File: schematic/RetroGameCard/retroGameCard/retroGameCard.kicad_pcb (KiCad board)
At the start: 2 copper layers, 34 parts, among them IC1 STM32C562KET6, J2 Conn_01x04_Pin, J3 USB_C_Receptacle_USB2.0_16P, SW1 SW_Slide_DPDT, SW2 SW_SPDT, SW3 SW_Push, SW4 SW_Push, SW5 SW_Push, SW6 SW_Push, SW7 SW_Push, U1 MCP73831-2-OT, U2 AP2112K-3.3

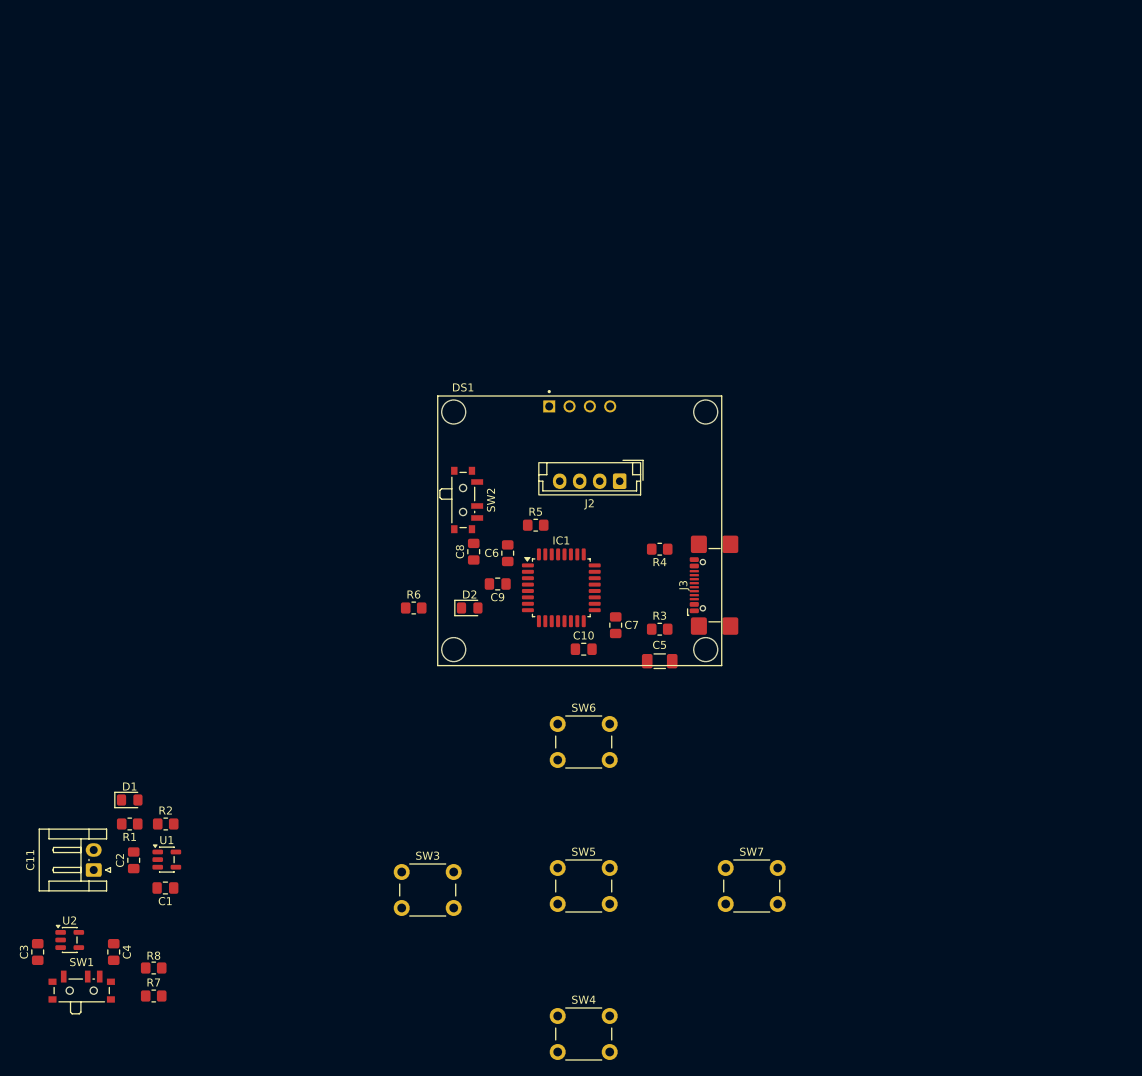
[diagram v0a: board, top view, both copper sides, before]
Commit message: changed layout
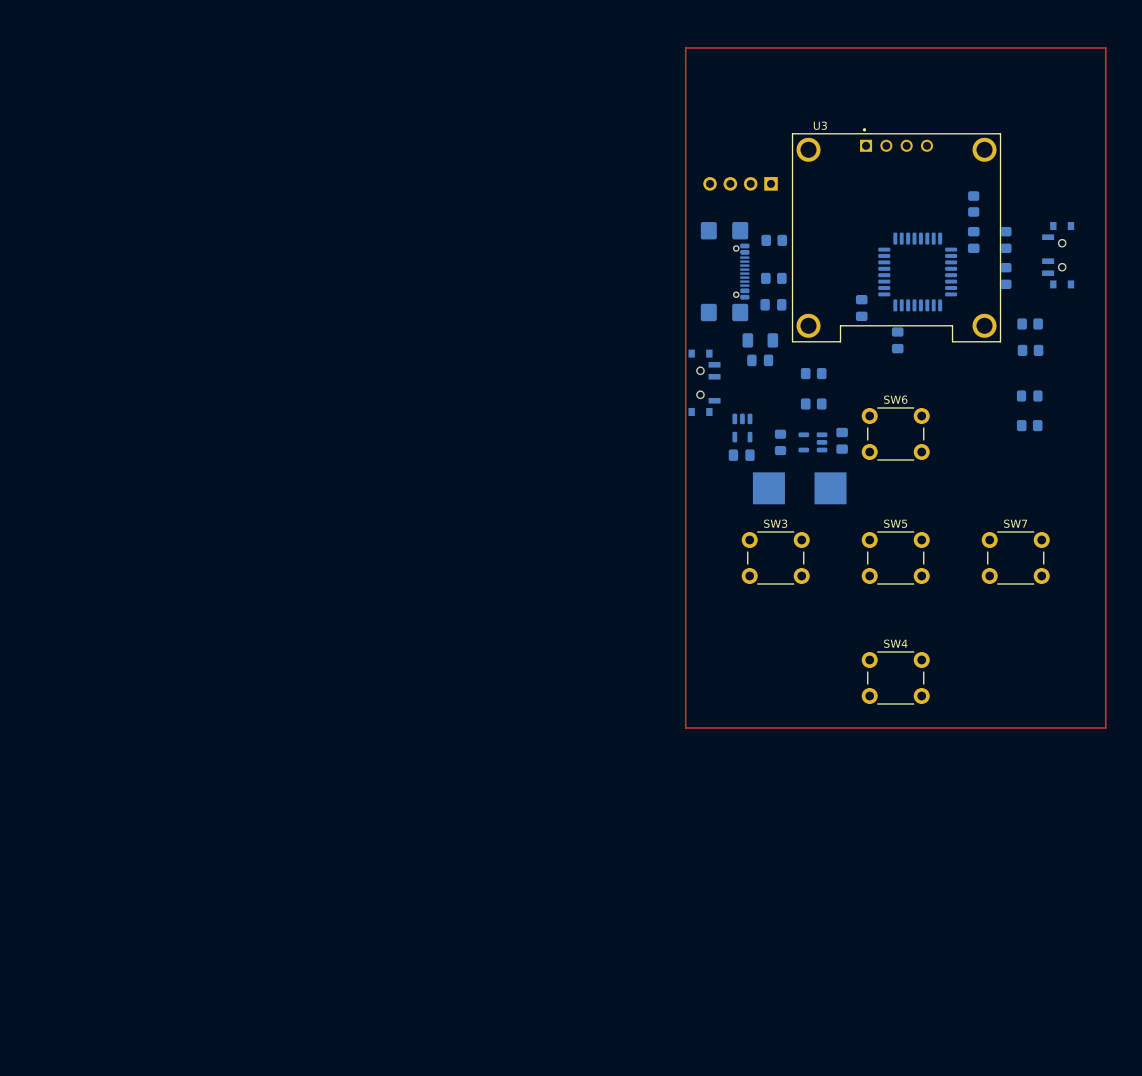
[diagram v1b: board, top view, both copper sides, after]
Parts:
- removed DS1: OLED_128X64_1.3_I2C, OLED_128X64_1.3_I2C:LCD_OLED_128X64_1.3_I2C
- added U3: DM-OLED096-636, OLED_128x64_0.96_I2C:MODULE_DM-OLED096-636, F.Cu at (215.3, 45.7)
- C1, C10, C2, C3, C4, C5, C6, C7, C8, C9, D1, D2, IC1, J3, R1, R2, R3, R4, R5, R6, R7, R8, SW1, SW2, U1, U2: moved to B.Cu
- C11: footprint Connector_JST:JST_EH_S2B-EH_1x02_P2.50mm_Horizontal -> TestPoint:Bez_nazwy_1; moved to B.Cu
- J2: footprint Connector_JST:JST_EH_B4B-EH-A_1x04_P2.50mm_Vertical -> Connector_PinHeader_2.54mm:PinHeader_1x04_P2.54mm_Horizontal; moved to B.Cu
- moved R7 136.1 mm to (232.1, 59.8)
- moved R8 135.9 mm to (232.1, 56.5)
- moved C3 116.7 mm to (198.3, 61.0), turned to 180 degrees
- moved SW1 108.4 mm to (191.2, 63.9), turned to 90 degrees
- moved U2 105.7 mm to (196.1, 69.5), turned to -90 degrees
- moved C1 105.3 mm to (200.0, 54.1), turned to 0 degrees
- moved C2 102.9 mm to (208.6, 71.1)
- moved R1 102.4 mm to (205.0, 62.7)
- moved C4 100.1 mm to (196.0, 72.9), turned to 0 degrees
- moved C11 99.2 mm to (203.6, 80.0), turned to 180 degrees
- moved R2 96.5 mm to (205.0, 66.5), turned to 180 degrees
- moved U1 96.1 mm to (204.9, 71.3), turned to 180 degrees
- moved D1 92.8 mm to (200.8, 71.3), turned to -90 degrees
- moved R6 80.3 mm to (232.0, 69.2)
- moved SW2 80.3 mm to (235.7, 47.9)
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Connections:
- J2 pad 2: /SWDIO -> /SWCLK
- J2 pad 3: /SWCLK -> /SWDIO

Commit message: update layout
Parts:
- moved C5 32.6 mm to (224.2, 38.6)
- moved U2 21.4 mm to (212.8, 56.2), turned to 180 degrees
- moved C4 21.1 mm to (208.8, 56.2), turned to -90 degrees
- moved C3 19.0 mm to (216.7, 56.4), turned to -90 degrees
- moved C2 16.0 mm to (196.2, 60.8)
- moved C11 15.1 mm to (202.2, 65.0), turned to 0 degrees
- moved D1 13.0 mm to (208.8, 61.0), turned to 90 degrees
- moved U1 11.8 mm to (199.7, 60.7), turned to 90 degrees
- moved SW2 9.89 mm to (233.2, 38.4)
- moved C9 7.63 mm to (224.7, 44.2), turned to 0 degrees
- moved C10 7.56 mm to (213.3, 51.3), turned to 180 degrees
- moved J2 7.01 mm to (204.1, 33.6), turned to 180 degrees
- moved R2 6.72 mm to (203.8, 59.9)
- moved C6 6.03 mm to (209.8, 48.6)
- moved IC1 5.74 mm to (216.5, 44.5)
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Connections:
- D2 pad 2: Net-(D2-A) -> /LED
- IC1 pad 12: /UP -> /LEFT
- IC1 pad 13: /RIGHT -> /UP
- IC1 pad 14: Net-(D2-A) -> unconnected-(IC1-PB0-Pad14)
- IC1 pad 8: unconnected-(IC1-PA2-Pad8) -> /LED
- IC1 pad 9: /LEFT -> /RIGHT

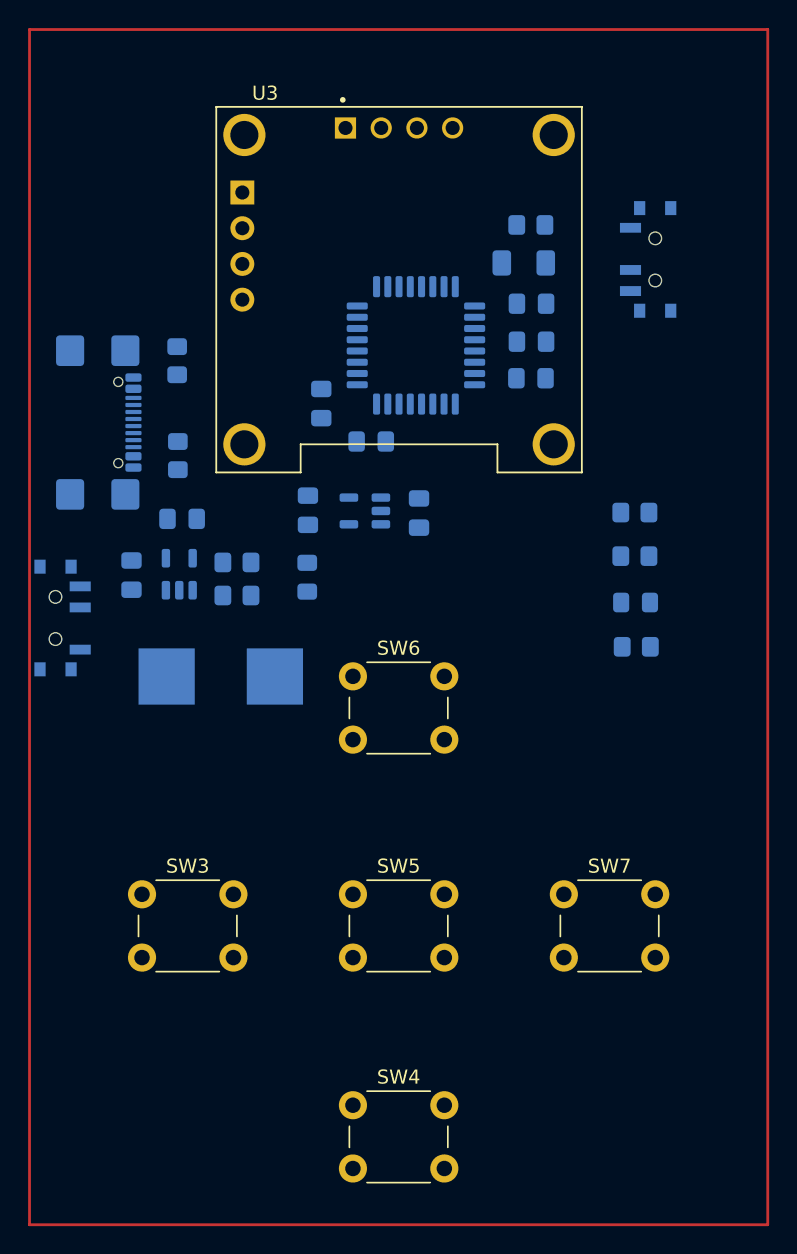
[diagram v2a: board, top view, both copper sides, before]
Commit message: added boundary of the pcb and holes for m3 screw
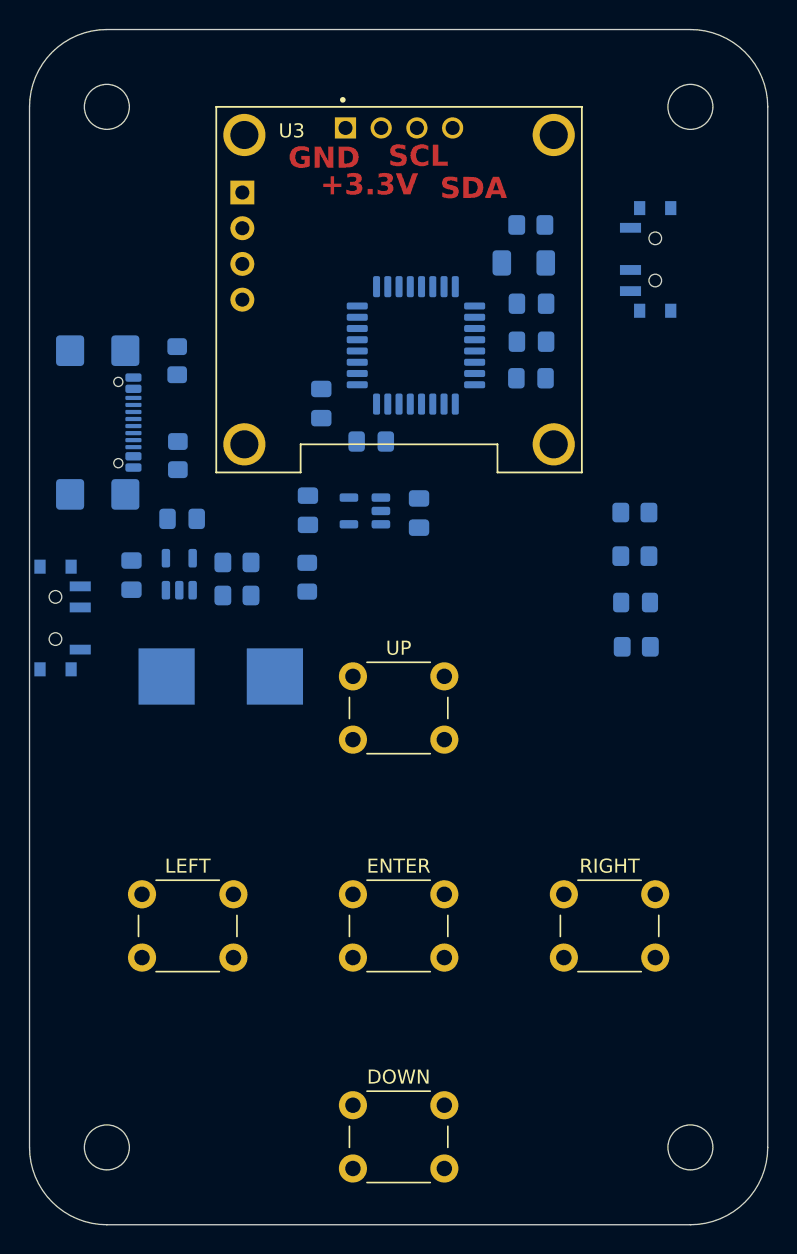
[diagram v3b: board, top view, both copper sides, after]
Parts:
- added H1: MountingHole, MountingHole:MountingHole_3.2mm_M3, F.Cu at (236.0, 27.5)
- added H2: MountingHole, MountingHole:MountingHole_3.2mm_M3, F.Cu at (194.5, 27.5)
- added H3: MountingHole, MountingHole:MountingHole_3.2mm_M3, F.Cu at (194.5, 101.5)
- added H4: MountingHole, MountingHole:MountingHole_3.2mm_M3, F.Cu at (236.0, 101.5)
- renumbered SW4 to DOWN, SW5 to ENTER, SW3 to LEFT, SW7 to RIGHT, SW6 to UP
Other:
- board outline added: 52.5 x 85 mm
- board text added: "+3.3V"
- board text added: "GND"
- board text added: "SCL"
- board text added: "SDA"

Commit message: added traces to PCB
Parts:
- moved R6 8.55 mm to (227.1, 59.0)
- moved D2 8.08 mm to (227.1, 56.4)
- moved C5 2.30 mm to (225.8, 40.2), turned to 90 degrees
- moved R7 2.28 mm to (234.3, 59.1)
- moved R8 2.15 mm to (234.2, 56.4)
- moved C7 1.89 mm to (223.1, 40.5), turned to 90 degrees
- moved U3 0.31 mm to (215.2, 40.8)
- renumbered LEFT to SW3, DOWN to SW4, ENTER to SW5, UP to SW6, RIGHT to SW7
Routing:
- net GND: track 0.00 -> 105.5 mm, vias 0 -> 33
- net /Vbat: track 0.00 -> 73.0 mm, vias 0 -> 4
- net /DOWN: track 0.00 -> 60.2 mm
- net /LEFT: track 0.00 -> 55.2 mm
- net Net-(U2-EN): track 0.00 -> 45.3 mm
- net /RIGHT: track 0.00 -> 44.6 mm
- net /ENTER: track 0.00 -> 44.4 mm
- net VBUS: track 0.00 -> 41.1 mm
- net +3.3V: track 0.00 -> 29.8 mm
- net /UP: track 0.00 -> 26.9 mm
- net /ADC_VBATT: track 0.00 -> 20.9 mm
- net /USB_D+: track 0.00 -> 18.4 mm
- net /USB_D-: track 0.00 -> 18.4 mm
- net /OLED_I2C_SDA: track 0.00 -> 11.5 mm
- net /LED: track 0.00 -> 11.4 mm
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- added copper zone on B.Cu, net /Vbat
- added copper zone on B.Cu, net GND
- added copper zone on F.Cu, net GND
- added copper zone on B.Cu, net VBUS
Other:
- board text added: "3.3V"
- board text added: "DEBUG"
- board text added: "SWCLK"
- board text added: "SWDIO"
